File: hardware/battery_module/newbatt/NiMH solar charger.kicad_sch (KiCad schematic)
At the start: 57 parts, among them J10 Conn_01x01_Socket, J11 Conn_01x01_Socket, J12 Conn_01x01_Socket, J13 Conn_02x03_Odd_Even, J3 Conn_01x01_Socket, J6 Conn_01x01_Socket, J7 Conn_01x01_Socket, J8 Conn_01x01_Socket, J9 Conn_01x01_Socket, Q1 NMOS, Q2 NMOS, Q3 NMOS, Q4 NMOS, U2 BQ25756ERRVR

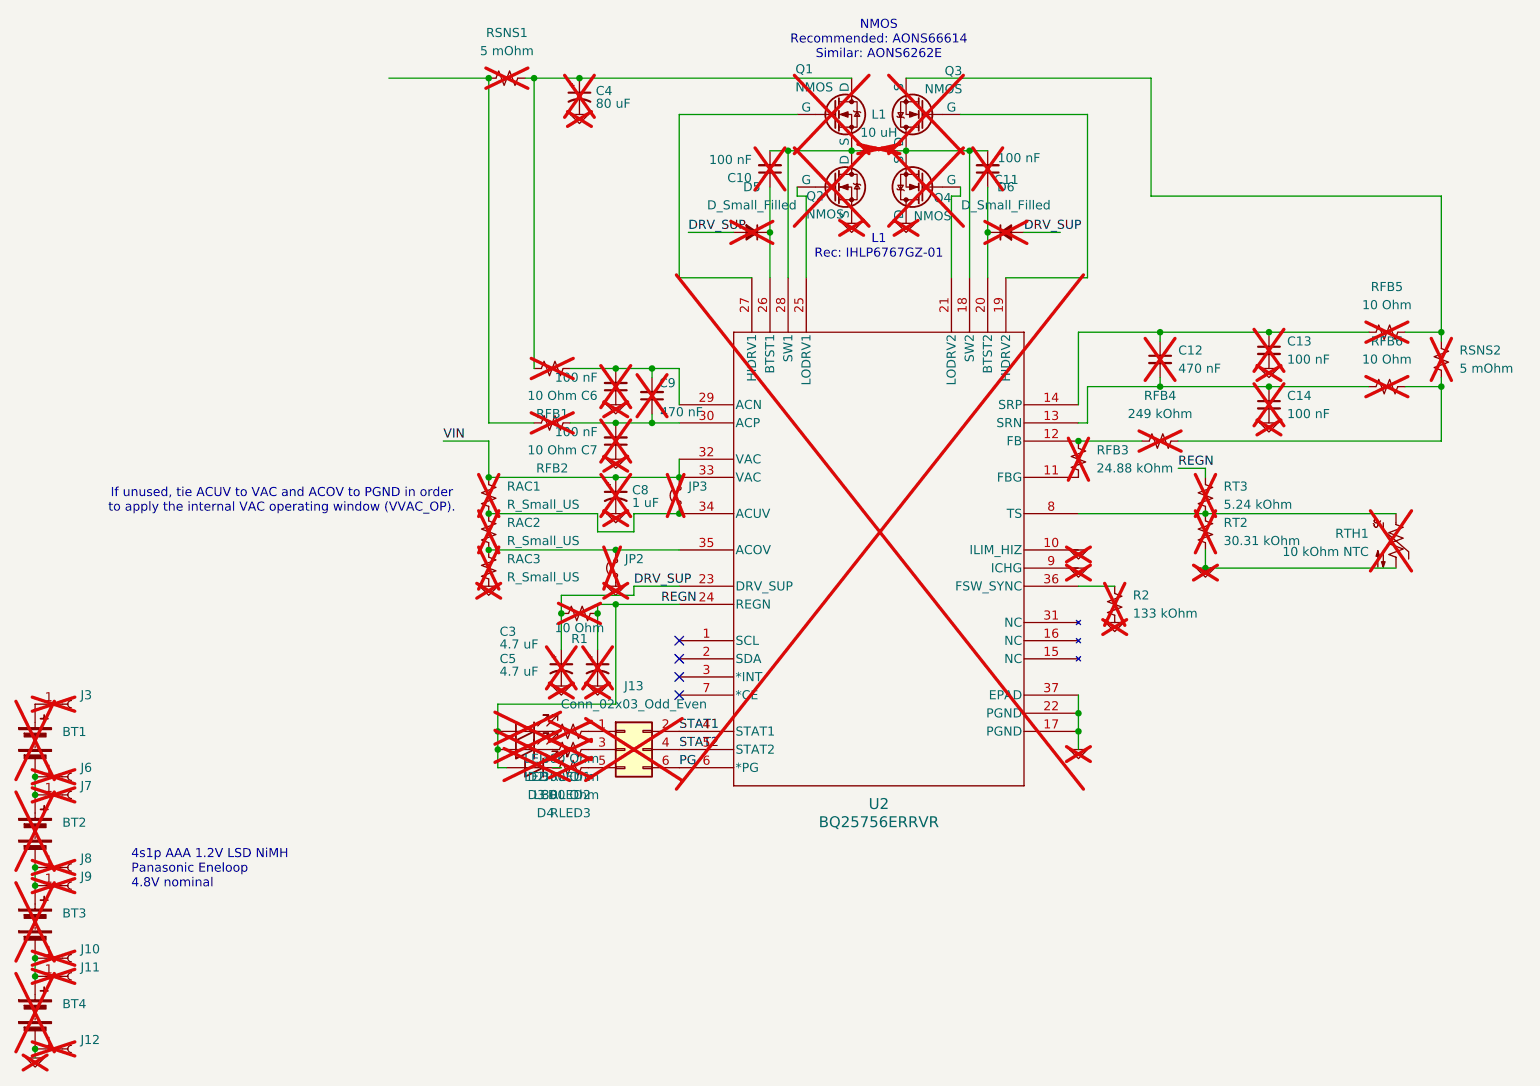
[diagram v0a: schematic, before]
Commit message: battery switch, fuse, and rerouted traces
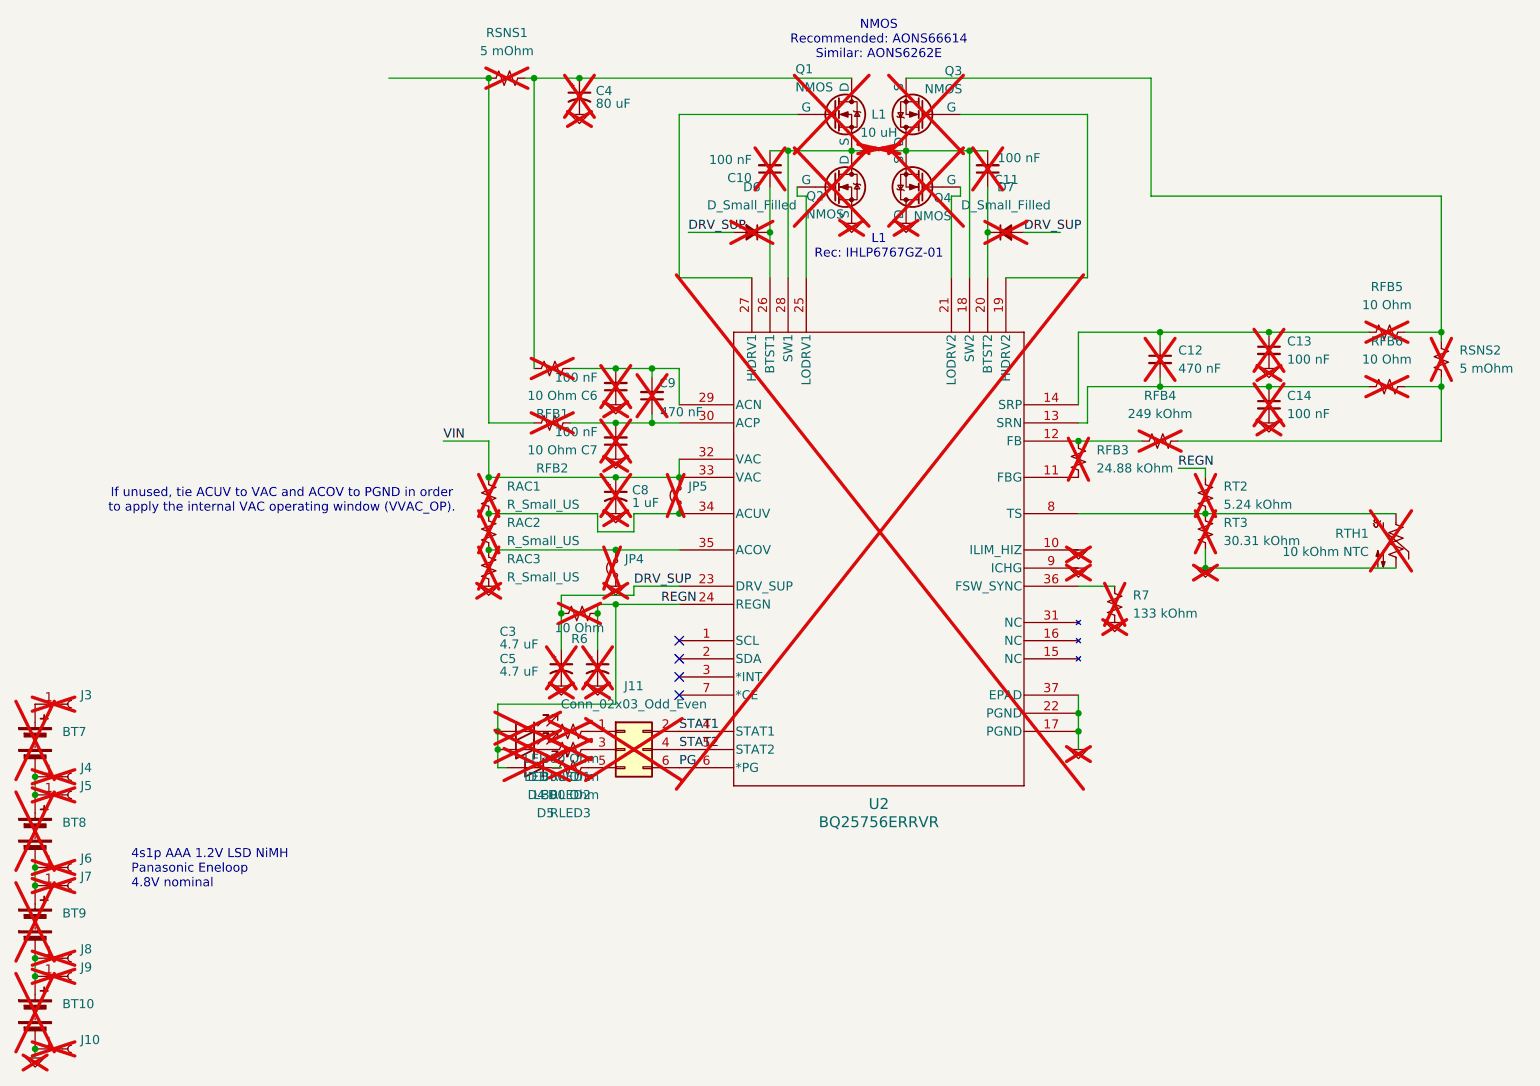
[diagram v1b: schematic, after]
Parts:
- renumbered BT4 to BT10, BT1 to BT7, BT2 to BT8, BT3 to BT9, D2 to D3, D3 to D4, D4 to D5, D5 to D6, D6 to D7, J12 to J10, J13 to J11, J6 to J4, J7 to J5, J8 to J6, J9 to J7, J10 to J8, J11 to J9, JP2 to JP4, JP3 to JP5, R1 to R6, R2 to R7, RT3 to RT2, RT2 to RT3

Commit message: Updated BoM with LCSC, Digikey. Updated 18650 battery clip footprint with 67.2mm spacing for 65mm and 67mm cells
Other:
- title: (none) -> ENTS Node Battery Module
